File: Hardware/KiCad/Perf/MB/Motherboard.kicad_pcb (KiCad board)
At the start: 2 copper layers, 96.5 x 71.1 mm, 61 parts, among them P1 Power input, P2 CONN_01X09, P3 CONN_01X05, P4 CONN_01X08, P5 CONN_02X03, P6 CONN_02X20, P7 CONN_02X20, P8 CONN_01X04, U1 STM32F100ZE, U2 LM29237-3.3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

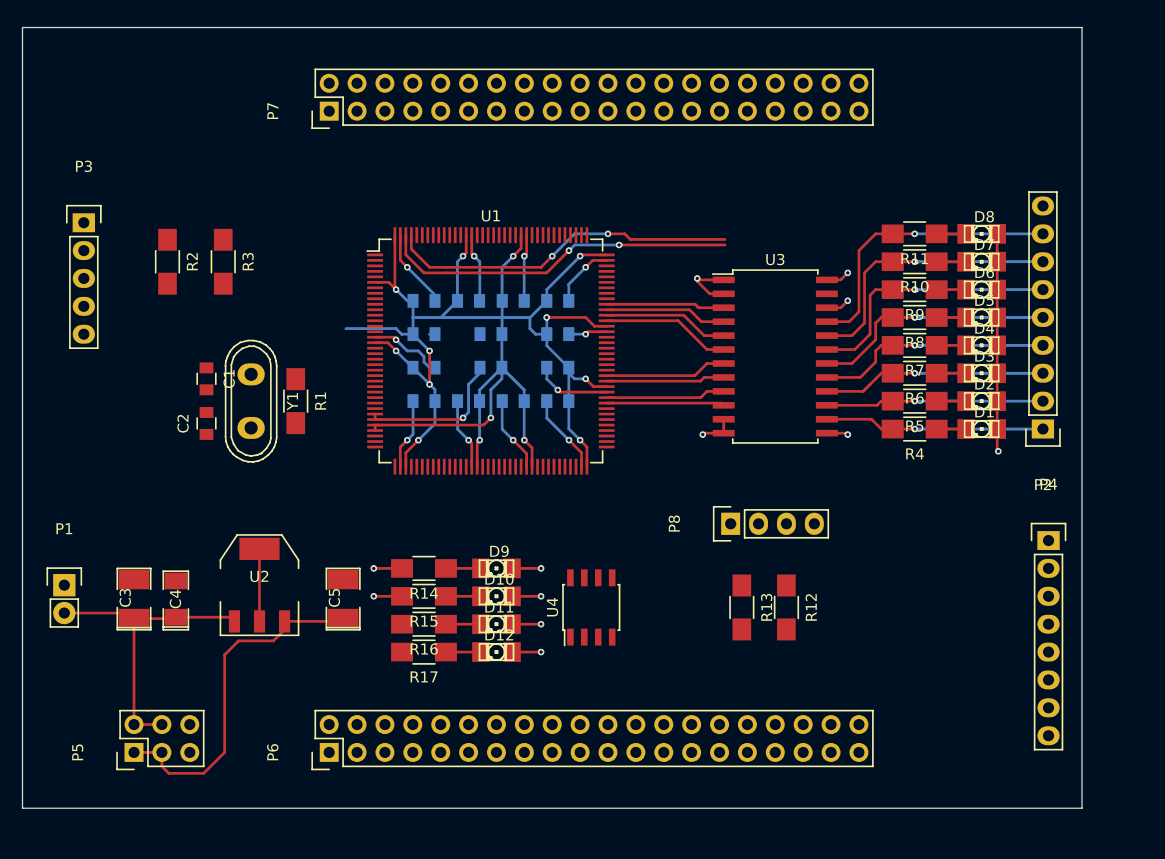
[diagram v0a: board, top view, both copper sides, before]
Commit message: laying out motherboard and backplane
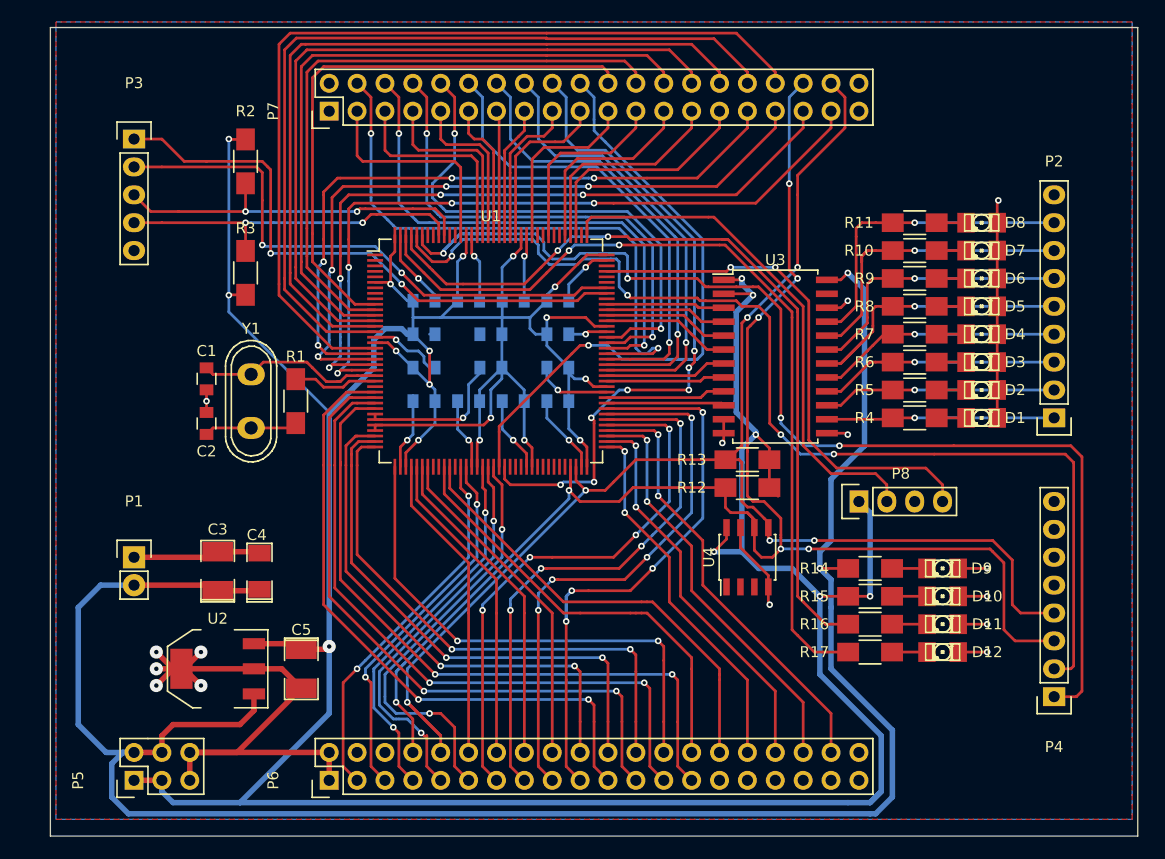
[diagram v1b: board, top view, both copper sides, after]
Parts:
- moved R14 40.6 mm to (186.4, 102.6)
- moved R15 40.6 mm to (186.4, 105.2)
- moved R16 40.6 mm to (186.4, 107.7)
- moved R17 40.6 mm to (186.4, 110.2)
- moved D10 40.6 mm to (193.0, 105.2)
- moved D11 40.6 mm to (193.0, 107.7)
- moved D12 40.6 mm to (193.0, 110.2)
- moved D9 40.6 mm to (193.0, 102.6)
- moved U4 14.9 mm to (175.3, 101.6)
- moved P4 14.2 mm to (203.2, 114.3), turned to 180 degrees
- moved R13 13.5 mm to (175.3, 92.7), turned to 180 degrees
- moved P8 11.9 mm to (185.4, 96.5)
- moved R2 11.6 mm to (129.5, 65.5)
- moved R12 11.5 mm to (175.3, 95.2), turned to 180 degrees
- moved P3 8.89 mm to (119.4, 63.5)
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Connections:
- P6 pad 11: USART 2 TX -> GPIO_15
- P6 pad 13: USART 2 RX -> USART 3 TX
- P6 pad 15: USART 2 CK -> USART 3 RX
- P6 pad 17: USART 3 TX -> USART 3 CK
- P6 pad 19: USART 3 RX -> USART 3 CTS
- P6 pad 20: UART 4 TX -> TIM 2 CH 1
- P6 pad 21: USART 3 CK -> ADC 10
- P6 pad 22: UART 4 RX -> TIM 2 CH 2
- P6 pad 23: USART 3 CTS -> ADC 11
- P6 pad 24: UART 5 TX -> TIM 2 CH 3
- P6 pad 25: GPIO_0 -> ADC 12
- P6 pad 26: UART 5 RX -> TIM 2 CH 4
- P6 pad 27: GPIO_1 -> ADC 13
- P6 pad 29: GPIO_2 -> Net-(P6-Pad29)
- P6 pad 3: GPIO_12 -> GPIO_11
- P6 pad 31: GPIO_3 -> Net-(P6-Pad31)
- P6 pad 33: GPIO_4 -> Net-(P6-Pad33)
- P6 pad 35: GPIO_5 -> Net-(P6-Pad35)
- P6 pad 37: GPIO_6 -> Net-(P6-Pad37)
- P6 pad 4: GPIO_10 -> Net-(P6-Pad4)
- P6 pad 5: GPIO_13 -> GPIO_12
- P6 pad 6: GPIO_11 -> Net-(P6-Pad6)
- P6 pad 7: GPIO_14 -> GPIO_13
- P6 pad 9: GPIO_15 -> GPIO_14
- P7 pad 10: GPIO_16 -> GPIO_24
- P7 pad 11: GPIO_25 -> GPIO_27
- P7 pad 12: GPIO_17 -> GPIO_20
- P7 pad 14: GPIO_18 -> GPIO_19
- P7 pad 15: GPIO_27 -> GPIO_25
- P7 pad 16: GPIO_19 -> GPIO_18
- P7 pad 17: GPIO_28 -> USART 2 CK
- P7 pad 18: GPIO_20 -> GPIO_17
- P7 pad 19: GPIO_29 -> USART 2 RX
- P7 pad 20: Net-(P7-Pad20) -> GPIO_16
- P7 pad 21: GPIO_30 -> USART 2 TX
- P7 pad 22: Net-(P7-Pad22) -> GPIO_0
- P7 pad 23: GPIO_31 -> UART 5 RX
- P7 pad 24: Net-(P7-Pad24) -> GPIO_1
- P7 pad 25: GPIO_7 -> UART 5 TX
- P7 pad 26: Net-(P7-Pad26) -> GPIO_2
- P7 pad 27: GPIO_8 -> UART 4 RX
- P7 pad 28: TIM 2 CH 1 -> GPIO_3
- P7 pad 29: GPIO_9 -> UART 4 TX
- P7 pad 3: GPIO_21 -> GPIO_31
- P7 pad 30: TIM 2 CH 2 -> GPIO_4
- P7 pad 31: ADC 10 -> GPIO_7
- P7 pad 32: TIM 2 CH 3 -> GPIO_5
- P7 pad 33: ADC 11 -> GPIO_8
- P7 pad 34: TIM 2 CH 4 -> GPIO_6
- P7 pad 35: ADC 12 -> GPIO_9
- P7 pad 37: ADC 13 -> GPIO_10
- P7 pad 4: Net-(P7-Pad4) -> GPIO_21
- P7 pad 5: GPIO_22 -> GPIO_30
- P7 pad 6: Net-(P7-Pad6) -> GPIO_22
- P7 pad 7: GPIO_23 -> GPIO_29
- P7 pad 8: Net-(P7-Pad8) -> GPIO_23
- P7 pad 9: GPIO_24 -> GPIO_28
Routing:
- net +3V3: track 187.6 -> 388.1 mm, vias 16 -> 23
- net +5V: track 32.8 -> 184.8 mm
- net I2C 2 SCL: track 0.00 -> 142.4 mm, vias 0 -> 7
- net I2C 2 SDA: track 0.00 -> 133.1 mm, vias 0 -> 6
- net TIM 16: track 0.00 -> 108.0 mm, vias 0 -> 4
- net TIM 17: track 0.00 -> 99.3 mm, vias 0 -> 4
- net GPIO_6: track 0.00 -> 81.7 mm
- net GPIO_5: track 0.00 -> 76.6 mm
- net GPIO_4: track 0.00 -> 71.8 mm
- net GND: track 129.3 -> 198.1 mm, vias 20 -> 27
- net GPIO_10: track 0.00 -> 67.5 mm, vias 0 -> 4
- net GPIO_3: track 0.00 -> 67.0 mm
- net GPIO_9: track 0.00 -> 66.2 mm, vias 0 -> 4
- net GPIO_8: track 0.00 -> 64.8 mm, vias 0 -> 4
- net GPIO_7: track 0.00 -> 63.0 mm, vias 0 -> 4
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- added copper zone on F.Cu, net (none)
- added copper zone on B.Cu, net GND
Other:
- board size 96.5 x 71.1 mm -> 99.1 x 73.7 mm
- net class power added: clearance 0.4, trace_width 0.5, via_dia 1.2, via_drill 0.4

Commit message: updated footprints and some layout
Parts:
- added ?: MountingHole_3-5mm, Mounting_Holes:MountingHole_3-5mm, F.Cu at (195.6, 58.4)
- added ?: MountingHole_3-5mm, Mounting_Holes:MountingHole_3-5mm, F.Cu at (195.6, 121.9)
- added ?: MountingHole_3-5mm, Mounting_Holes:MountingHole_3-5mm, F.Cu at (116.8, 58.4)
- added ?: MountingHole_3-5mm, Mounting_Holes:MountingHole_3-5mm, F.Cu at (116.8, 121.9)
- P1: footprint Pin_Headers:Pin_Header_Straight_1x02 -> perfFoot:ph_2p_ang
- P2: value CONN_01X09 -> CONN_01X10; footprint Pin_Headers:Pin_Header_Straight_1x09 -> perfFoot:ph_10p_ang
- P3: footprint Pin_Headers:Pin_Header_Straight_1x05 -> perfFoot:ph_5p_ang
- P4: value CONN_01X08 -> CONN_01X05; footprint Pin_Headers:Pin_Header_Straight_1x08 -> perfFoot:ph_5p_ang
- moved P2 10.2 mm to (203.2, 78.7), turned to 90 degrees
- moved P3 10.2 mm to (119.4, 73.7), turned to 270 degrees
- moved P5 7.62 mm to (127.0, 121.9)
- moved P4 2.54 mm to (203.2, 111.8), turned to 90 degrees
- moved P1 1.27 mm to (119.4, 102.9), turned to 270 degrees
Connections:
- P2 pad 9: GND -> Net-(P2-Pad9)
- P4 pad 5: Net-(P4-Pad5) -> GND
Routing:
- net GND: track 198.1 -> 178.4 mm
- net +5V: track 184.8 -> 168.4 mm
- net +3V3: track 388.1 -> 377.6 mm
- net USART 1 RX: track 52.0 -> 47.3 mm
- net Net-(P2-Pad1): track 19.7 -> 23.6 mm
- net Net-(P2-Pad2): track 20.3 -> 23.6 mm
- net Net-(P2-Pad3): track 20.8 -> 23.6 mm
- net I2C 2 SCL: track 142.4 -> 145.0 mm
- net Net-(P2-Pad4): track 21.9 -> 24.2 mm
- net GPIO_21: track 53.9 -> 51.8 mm
- net I2C 1 SMBA: track 33.0 -> 34.9 mm, vias 2 -> 3
- net Net-(P2-Pad8): track 27.6 -> 29.4 mm
- net Net-(P2-Pad5): track 26.8 -> 28.7 mm
- net USART 1 TX: track 53.9 -> 52.4 mm
- net TIM 17: track 99.3 -> 97.8 mm
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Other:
- board text added: "3.3V"
- board text added: "5V"
- board text added: "AUX0"
- board text added: "COM"
- board text added: "GND"
- board text added: "Power"
- board text added: "SYS"
- board text added: "THRUSTER"

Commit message: updated BOM
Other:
- board text added: "1"

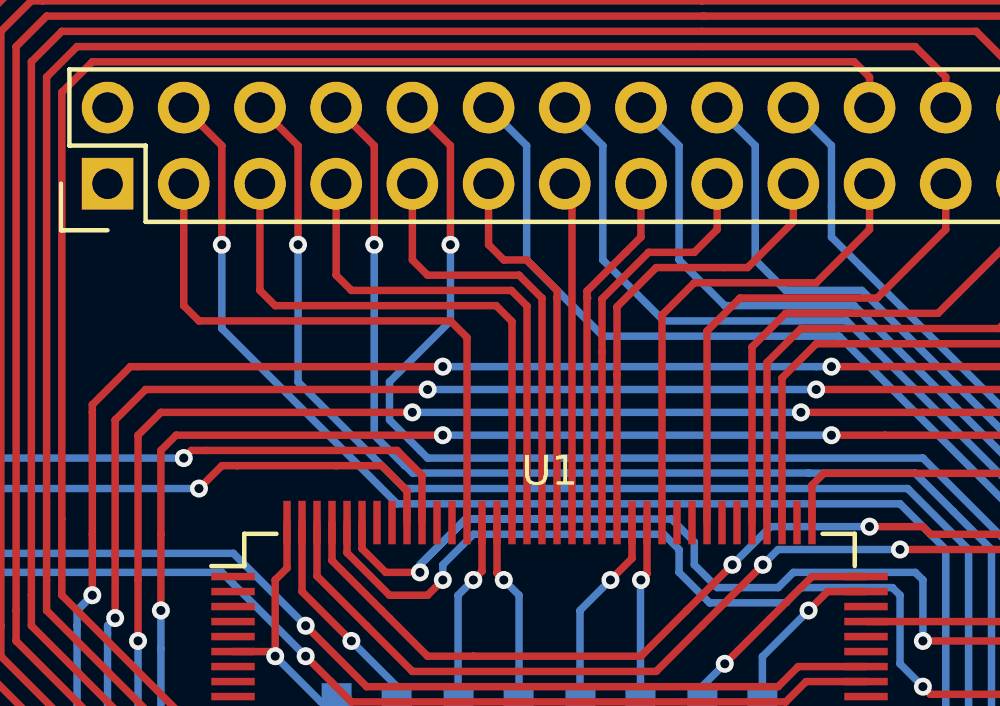
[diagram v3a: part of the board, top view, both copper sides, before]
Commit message: Small change to USART 2 pin layout from MB to Backplane
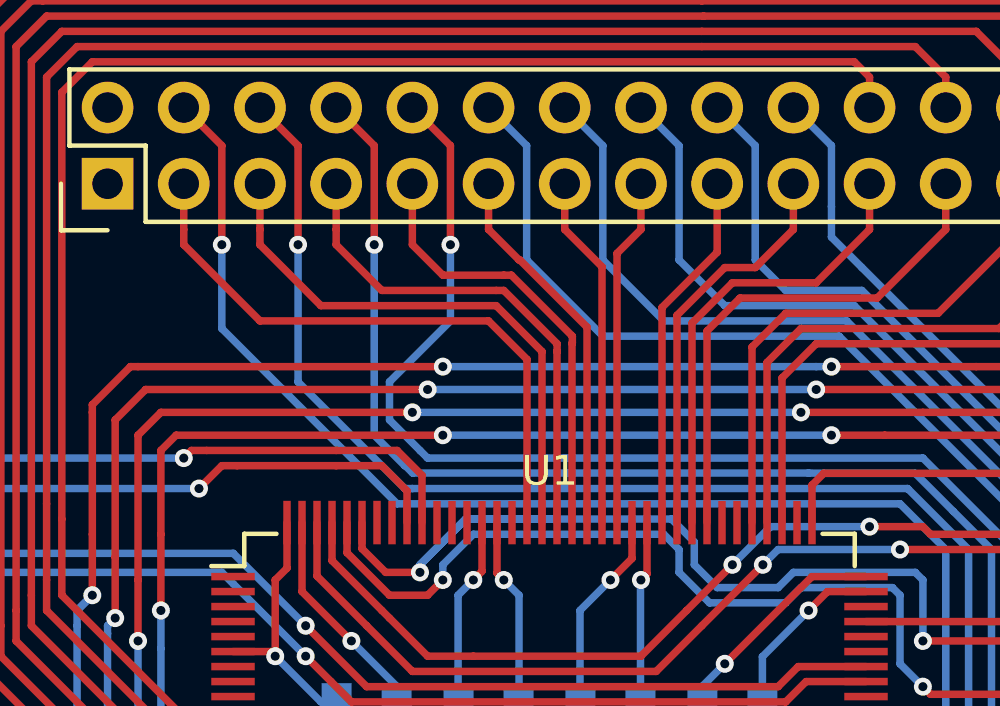
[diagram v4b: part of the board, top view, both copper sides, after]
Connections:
- P7 pad 11: GPIO_27 -> GPIO_25
- P7 pad 13: GPIO_26 -> USART 2 CK
- P7 pad 15: GPIO_25 -> USART 2 RX
- P7 pad 17: USART 2 CK -> USART 2 TX
- P7 pad 19: USART 2 RX -> USART 2 RTS
- P7 pad 21: USART 2 TX -> USART 2 CTS
- P7 pad 3: GPIO_31 -> GPIO_29
- P7 pad 5: GPIO_30 -> GPIO_28
- P7 pad 7: GPIO_29 -> GPIO_27
- P7 pad 9: GPIO_28 -> GPIO_26
- U1 pad 117: Net-(U1-Pad117) -> USART 2 CTS
- U1 pad 118: Net-(U1-Pad118) -> USART 2 RTS
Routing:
- net GPIO_31: track 20.1 -> 0.00 mm
- net GPIO_30: track 19.1 -> 0.00 mm
- net USART 2 CTS: track 0.00 -> 15.4 mm
- net USART 2 RTS: track 0.00 -> 13.5 mm
- net USART 2 TX: track 16.5 -> 12.1 mm
- net GPIO_27: track 12.7 -> 16.7 mm
- net USART 2 RX: track 15.5 -> 11.6 mm
- net GPIO_28: track 14.9 -> 18.6 mm
- net GPIO_26: track 11.4 -> 14.8 mm
- net GPIO_29: track 17.1 -> 20.5 mm
- net USART 2 CK: track 13.8 -> 12.2 mm
- net GPIO_25: track 12.1 -> 12.7 mm

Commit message: updated error in level shifter footprint
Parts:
- U3: footprint Housings_SOIC:SOIC-24_7.5x15.4mm_Pitch1.27mm -> Housings_SSOP:TSSOP-24_4.4x7.8mm_Pitch0.65mm
- moved R14 1.52 mm to (184.9, 102.6)
- moved R15 1.52 mm to (184.9, 105.2)
- moved R16 1.52 mm to (184.9, 107.7)
- moved R17 1.52 mm to (184.9, 110.2)
- moved U3 1.52 mm to (176.3, 83.3)
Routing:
- net +3V3: track 377.6 -> 369.7 mm, vias 23 -> 22
- net Net-(P2-Pad1): track 23.6 -> 29.1 mm
- net Net-(P2-Pad4): track 24.2 -> 28.7 mm
- net Net-(P2-Pad3): track 23.6 -> 28.0 mm
- net GND: track 178.4 -> 174.1 mm, vias 27 -> 25
- net Net-(P2-Pad7): track 28.5 -> 32.2 mm
- net Net-(P2-Pad8): track 29.4 -> 33.0 mm
- net Net-(P2-Pad2): track 23.6 -> 26.8 mm
- net Net-(P2-Pad6): track 26.5 -> 29.4 mm
- net INT_GPIO_0: track 74.1 -> 76.1 mm, vias 2 -> 4
- net JTMS-SWDIO: track 47.9 -> 49.6 mm, vias 2 -> 4
- net Net-(D9-Pad1): track 3.18 -> 4.71 mm
- net Net-(D12-Pad1): track 3.18 -> 4.71 mm
- net Net-(D11-Pad1): track 3.18 -> 4.71 mm
- net Net-(D10-Pad1): track 3.18 -> 4.71 mm
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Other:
- board text added: "CLK"
- board text added: "DIO"
- board text added: "SWD"
- board text added: "UiS Subsea PERF - Motherboard V1.0 Designed by: Sletten"

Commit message: Fixed missign ground connection to level shifter
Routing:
- net GND: track 174.1 -> 176.8 mm, vias 25 -> 27

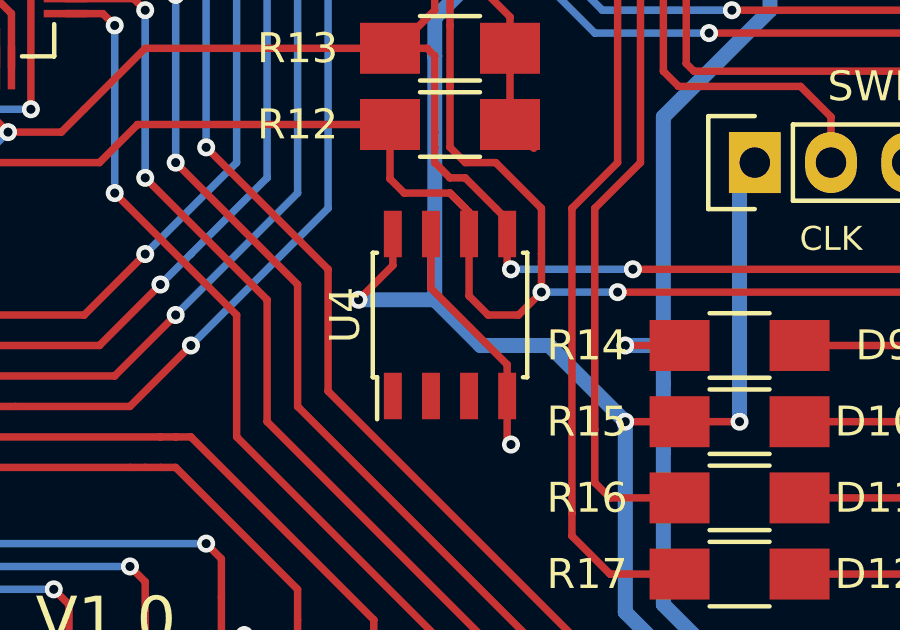
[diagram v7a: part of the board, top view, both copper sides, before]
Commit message: fixed adressing error on PERF eeprom
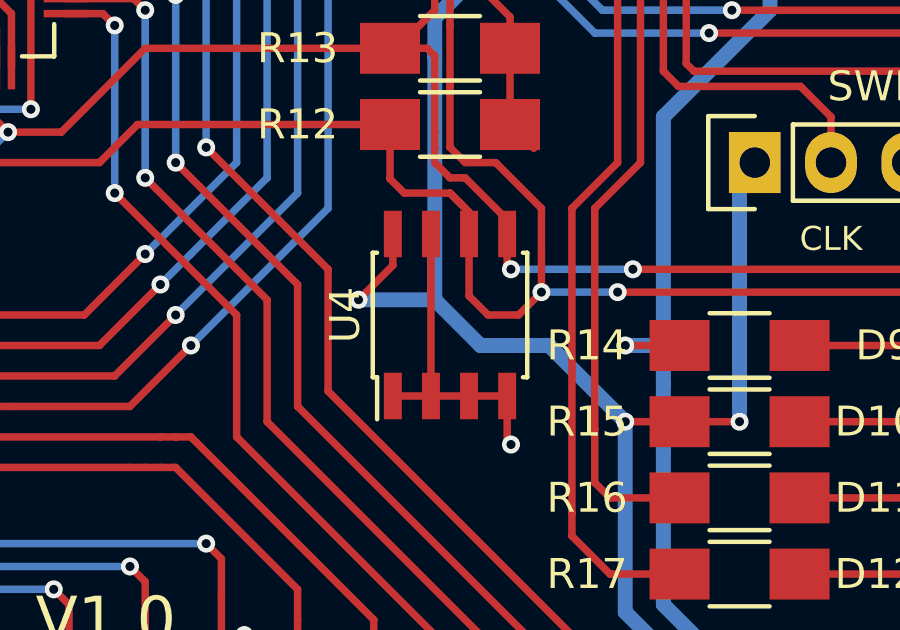
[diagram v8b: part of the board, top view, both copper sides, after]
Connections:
- U4 pad 1: Net-(U4-Pad1) -> GND
- U4 pad 2: Net-(U4-Pad2) -> GND
- U4 pad 3: Net-(U4-Pad3) -> GND
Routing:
- net GND: track 176.8 -> 179.5 mm
